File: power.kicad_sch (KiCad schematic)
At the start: 48 parts, among them IC302 L7805, IC303 L7805, J101 Test Points, P301 POWER, P302 POWER, Q106 15 29, Q304 BR 30, Q308 FR 32, Q503 BR 29, SW101 SW_SPDT

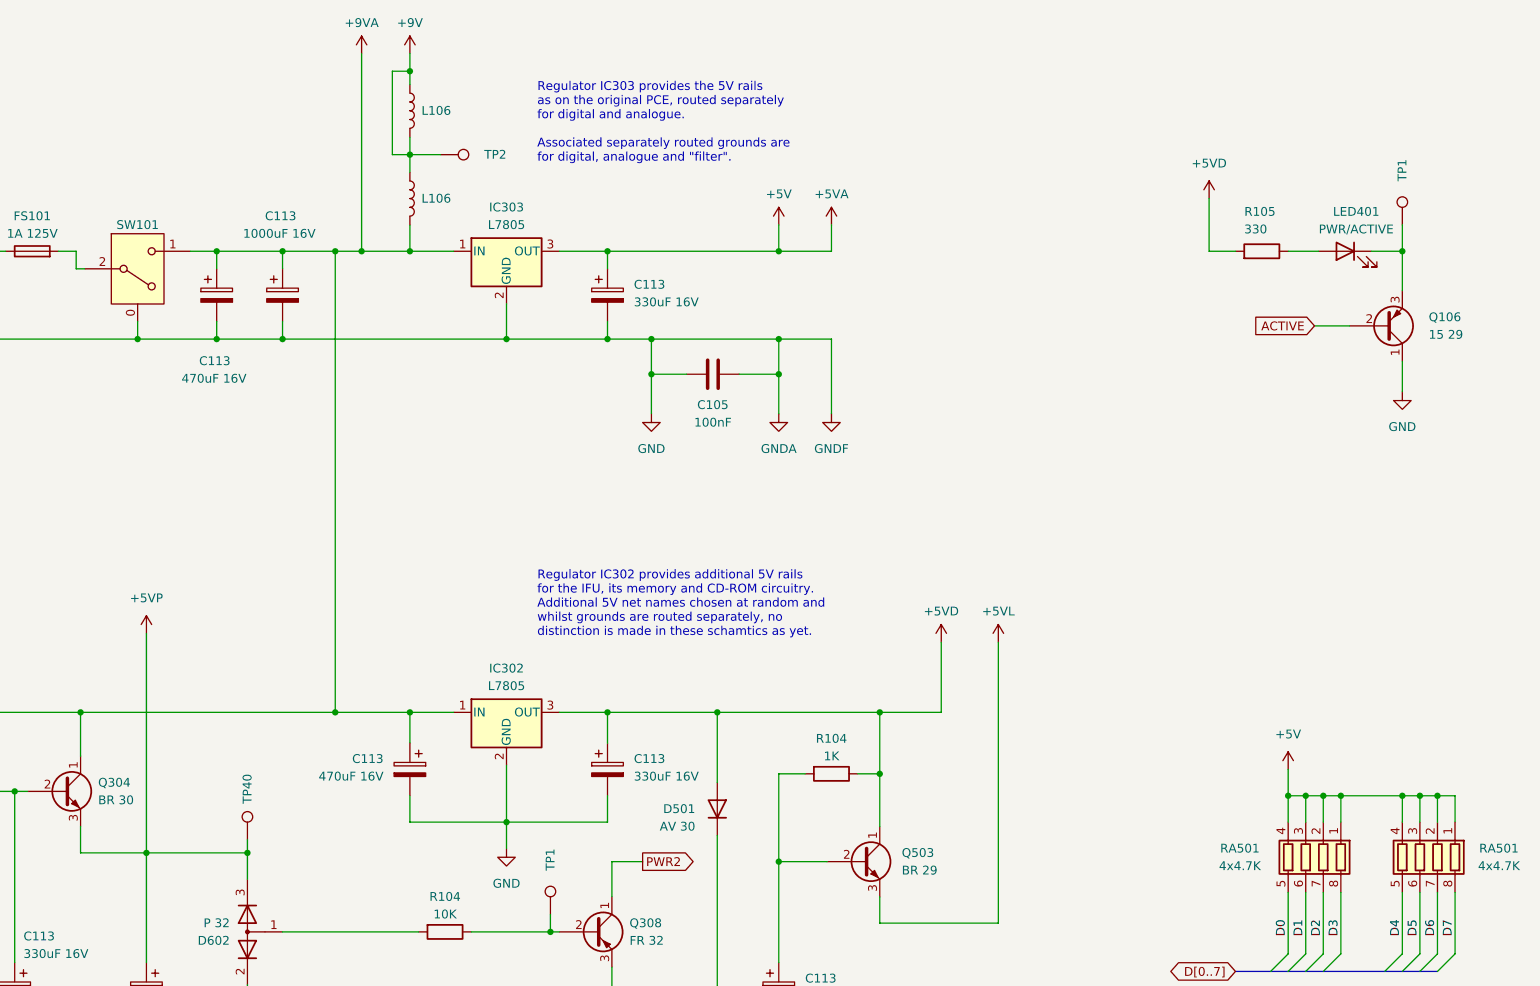
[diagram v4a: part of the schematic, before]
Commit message: Minor schematic/silkscreen changes.
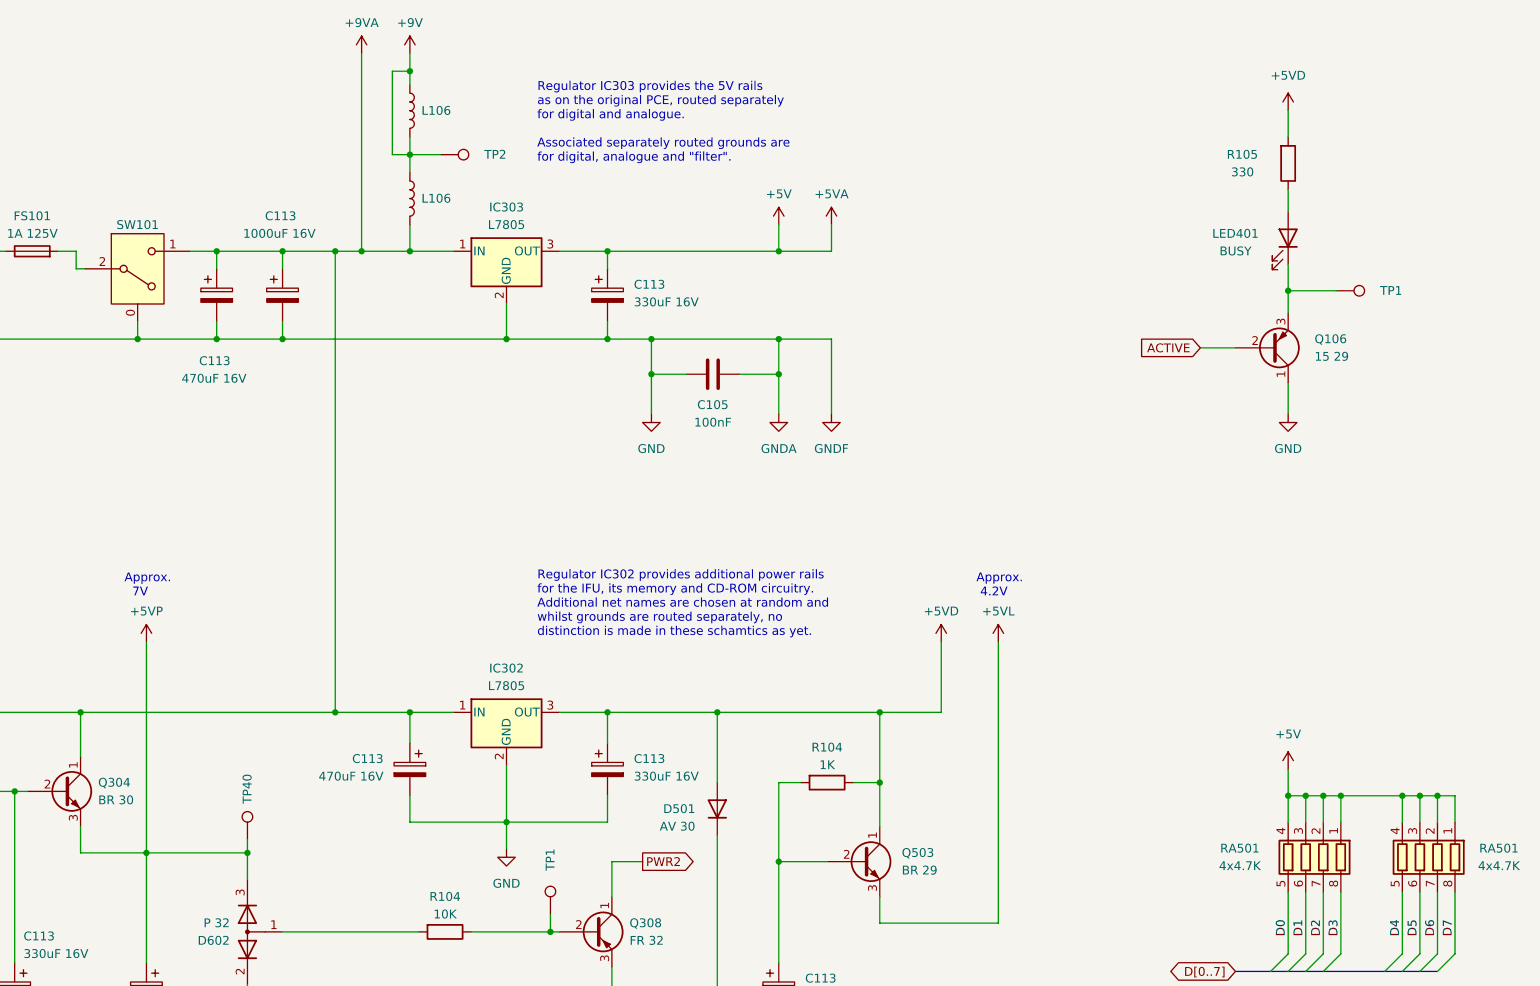
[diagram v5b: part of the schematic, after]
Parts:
- FL301: now left out of the parts list
- LED401: value PWR/ACTIVE -> BUSY
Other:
- note added: "Approx. 4.2V"
- note added: "Approx. 7V"
- note added: "Regulator IC302 provides additional power rails for the IFU, its memory and CD-ROM circuitry. Additional net names are chosen at random and whilst grounds are routed separately, no distinction is made in these schamtics as yet."
- note removed: "Regulator IC302 provides additional 5V rails for the IFU, its memory and CD-ROM circuitry. Additional 5V net names chosen at random and whilst grounds are routed separately, no distinction is made in these schamtics as yet."
- moved on the sheet: LED401, Q106, R104, R105, TP1

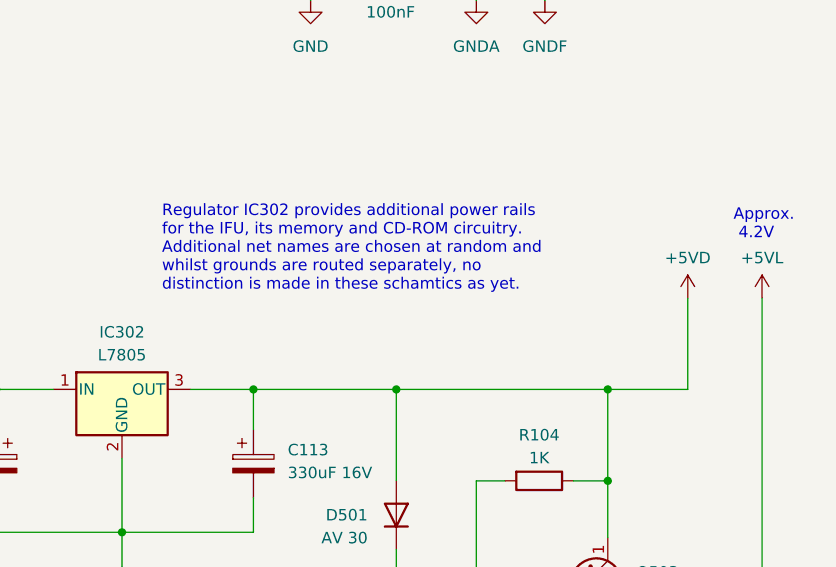
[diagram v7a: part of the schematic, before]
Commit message: Correct typos in schematics.
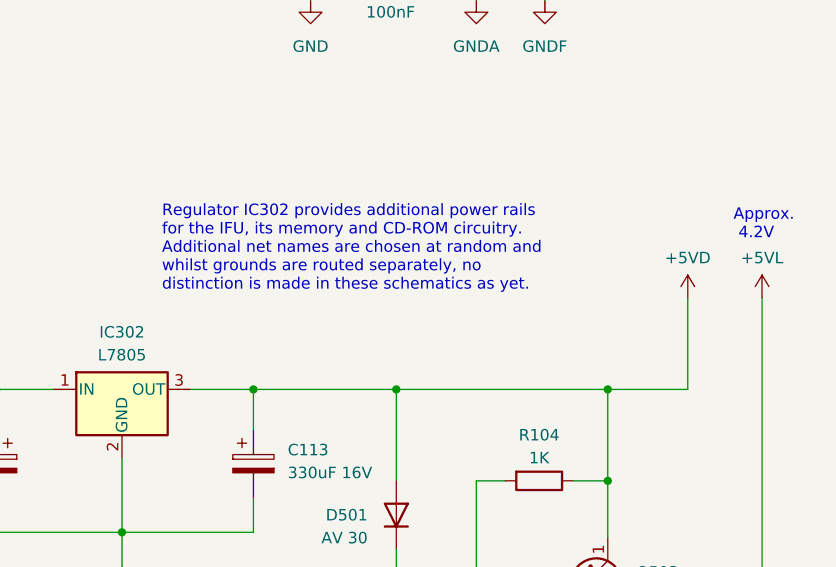
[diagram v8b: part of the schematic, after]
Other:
- note added: "Regulator IC302 provides additional power rails for the IFU, its memory and CD-ROM circuitry. Additional net names are chosen at random and whilst grounds are routed separately, no distinction is made in these schematics as yet."
- note removed: "Regulator IC302 provides additional power rails for the IFU, its memory and CD-ROM circuitry. Additional net names are chosen at random and whilst grounds are routed separately, no distinction is made in these schamtics as yet."
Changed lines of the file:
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@@
     (effects (font (size 1.27 1.27)) (justify left bottom))
   )
-  (text "Regulator IC302 provides additional power rails\nfor the IFU, its memory and CD-ROM circuitry.\nAdditional net names are chosen at random and\nwhilst grounds are routed separately, no\ndistinction is made in these schamtics as yet."
+  (text "Regulator IC302 provides additional power rails\nfor the IFU, its memory and CD-ROM circuitry.\nAdditional net names are chosen at random and\nwhilst grounds are routed separately, no\ndistinction is made in these schematics as yet."
     (at 241.3 117.475 0)
-    (effects (font (size 1.27 1.27)) (justify left bottom))
+    (effects (font (size 1.27 1.27)) (justify left bottom) (href "#4"))
   )
   (text "Approx.\n  7V" (at 181.61 111.76 0)
